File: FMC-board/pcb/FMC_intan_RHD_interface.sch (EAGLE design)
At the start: 84 parts, among them Q1 SSM3J328R, U1 4901, U2 7933, U3 ADN4663, U4 ADN4663, U5 ADN4664, U6 PDS1, U7 4901, U8 FMC_SINGLE_WIDTH_MODULE

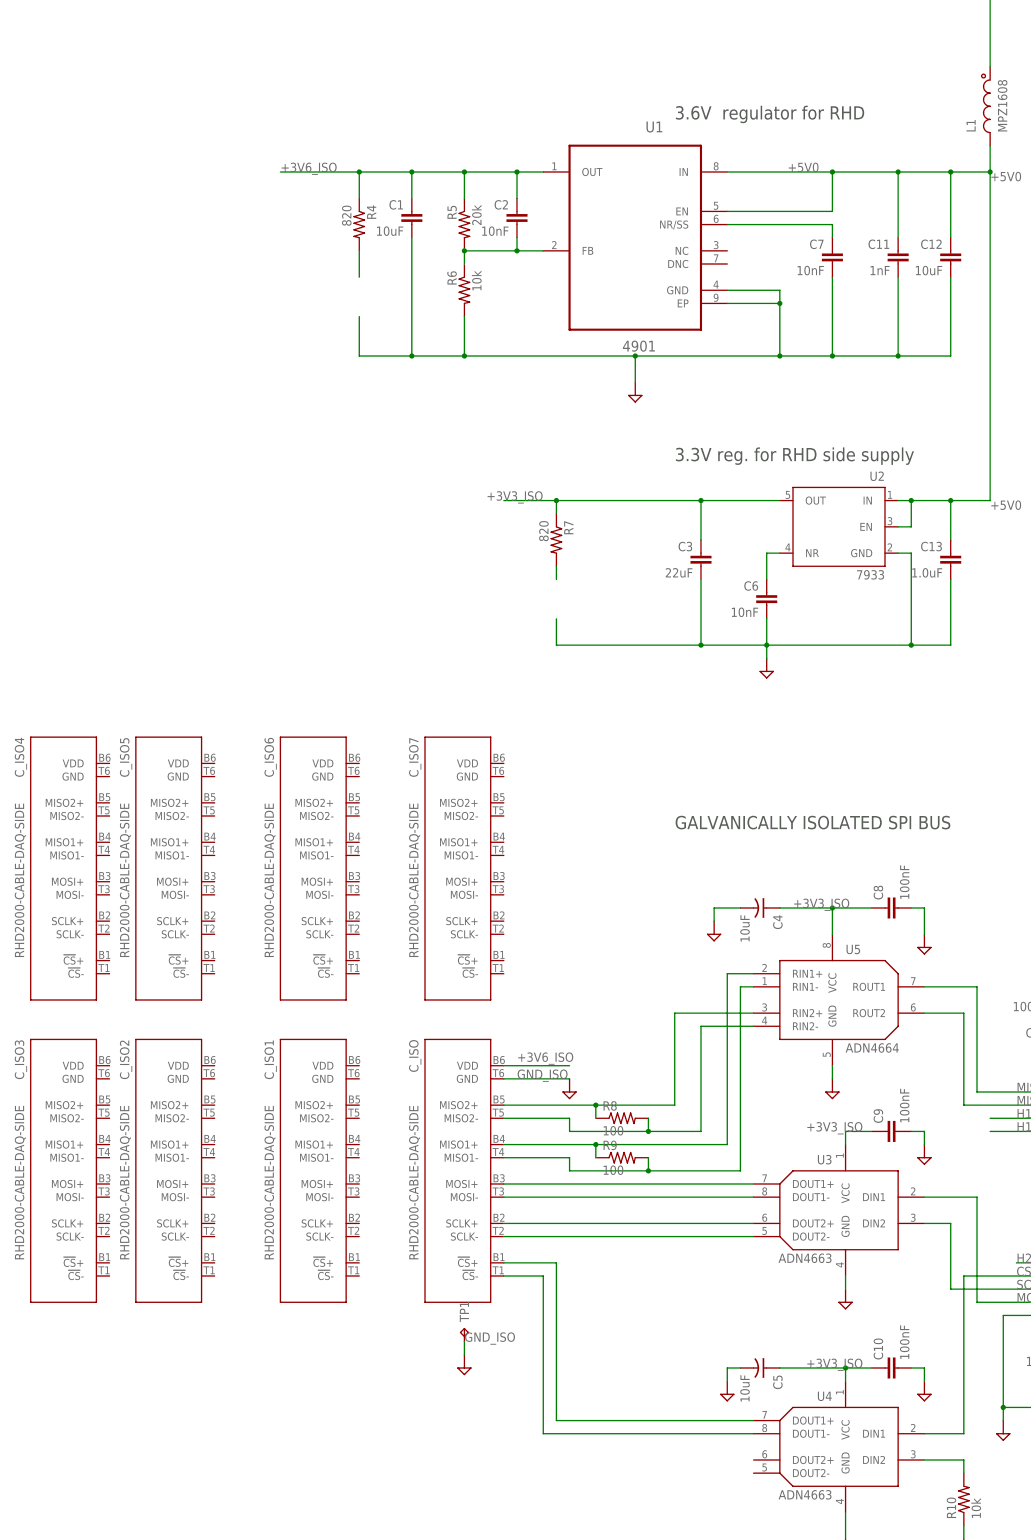
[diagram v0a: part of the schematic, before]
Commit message: added some cmos/lvds bridge components to check spacing
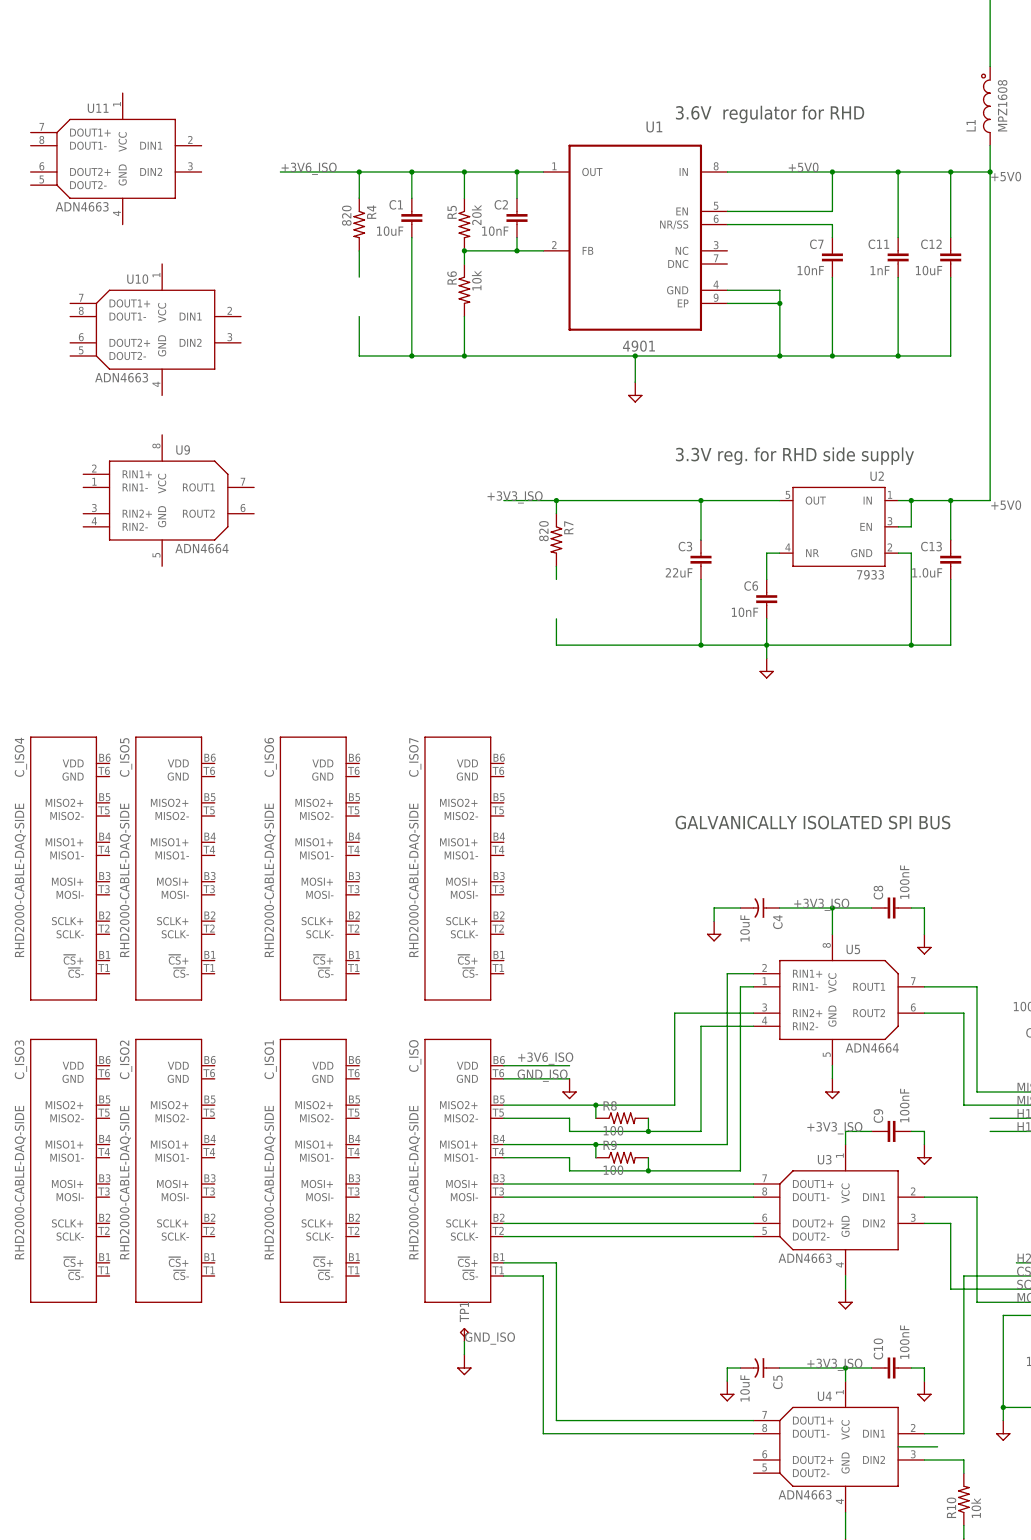
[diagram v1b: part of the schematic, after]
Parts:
- added U10, U11: ADN4663, jonnew:ADN4663_SOIC
- added U9: ADN4664, jonnew:ADN4664_SOIC
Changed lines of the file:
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@@
 <part name="DO_ISO2" library="jonnew" deviceset="ADUM3440" device="" value="ISO7640"/>
 <part name="DI_ISO2" library="jonnew" deviceset="ADUM3440" device="" value="ISO7640"/>
+<part name="U9" library="jonnew" deviceset="ADN4664" device="_SOIC" value="ADN4664"/>
+<part name="U10" library="jonnew" deviceset="ADN4663" device="_SOIC" value="ADN4663"/>
+<part name="U11" library="jonnew" deviceset="ADN4663" device="_SOIC" value="ADN4663"/>
 </parts>
 <sheets>
@@
 <instance part="DO_ISO2" gate="G$1" x="228.6" y="66.04" rot="R180"/>
 <instance part="DI_ISO2" gate="G$1" x="228.6" y="88.9"/>
+<instance part="U9" gate="G$1" x="33.02" y="287.02"/>
+<instance part="U10" gate="G$1" x="27.94" y="317.5" rot="MR0"/>
+<instance part="U11" gate="G$1" x="20.32" y="350.52" rot="MR0"/>
 </instances>
 <busses>
@@
 <pinref part="U4" gate="G$1" pin="DIN1"/>
 <wire x1="185.42" y1="109.22" x2="177.8" y2="109.22" width="0.1524" layer="91"/>
-</segment>
-</net>
+<wire x1="180.34" y1="106.68" x2="172.72" y2="106.68" width="0.1524" layer="91"/>
+</segment>
+</net>

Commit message: basic layout concept for 8 SPI interfaces on one FMC carrier
using existing parts, but utilizing both sides of the PCB
only added 4 ports for now to evaluate the basic stragety
there are a lot of traces that need to be split etc.
will have to switch to flatter DC-DC for this
also check if we can use 2 power supplies for 8 posrts or if we need to bump up the current capacity.
might be able to expand the back of the pcb outline behind the FMC a bit and stay within the vita spec?
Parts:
- removed C_ISO, C_ISO5, C_ISO6, C_ISO7: RHD2000-CABLE-DAQ-SIDE, RHD2000_eval_board:RHD2000-CABLE-DAQ-SIDE
- removed DI_ISO, DO_ISO: ISO7640, jonnew:ADUM3440
- removed TP1: GND-ISO, jonnew:TPPAD1-13
- removed TP_CS: CS, jonnew:TPTP06R
- removed TP_H1: H23, jonnew:TPTP06R
- removed TP_H2: H14, jonnew:TPTP06R
- removed TP_H3: H13, jonnew:TPTP06R
- removed TP_MISO1: MISO1, jonnew:TPTP06R
- removed TP_MISO2: MISO2, jonnew:TPTP06R
- removed TP_MOSI: MOSI, jonnew:TPTP06R
- removed TP_SCLK: SCLK, jonnew:TPTP06R
- added C33, C34, C35, C36, C37, C38, C39, C42, C43, C44, C47, C48, C49, C50: 100nF, RHD2000_eval_board:C_0603
- added C40, C41, C45, C46, C51: 10uF, jonnew:C-POL_1206
- added DI_ISO3, DI_ISO4: ISO7640, jonnew:ADUM3440
- added R1, R14, R15, R2, R3: 100, RHD2000_eval_board:R_0603
- added U12: ADN4664, jonnew:ADN4664_SOIC
- added U13, U14, U15: ADN4663, jonnew:ADN4663_SOIC
- C17: value 100nF -> 10uF; device RHD2000_eval_board:C_0603 -> jonnew:C-POL_1206
- C4, C5: value 10uF -> 100nF; device jonnew:C-POL_1206 -> RHD2000_eval_board:C_0603
- R10: value 10k -> 100; device jonnew:R_0603 -> RHD2000_eval_board:R_0603
- U11, U3: value ADN4663 -> ADN4664; device jonnew:ADN4663_SOIC -> jonnew:ADN4664_SOIC
- U9: value ADN4664 -> ADN4663; device jonnew:ADN4664_SOIC -> jonnew:ADN4663_SOIC
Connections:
- removed net CS+_ISOLATED: C_ISO.!CS!+, U4.DOUT1+
- removed net CS-_ISOLATED: C_ISO.!CS!-, U4.DOUT1-
- removed net MISO1+_ISOLATED: C_ISO.MISO1+, R9.1, U5.RIN1+
- removed net MISO1-_ISOLATED: C_ISO.MISO1-, R9.2, U5.RIN1-
- removed net MISO2+_ISOLATED: C_ISO.MISO2+, R8.1, U5.RIN2+
- removed net MISO2-_ISOLATED: C_ISO.MISO2-, R8.2, U5.RIN2-
- removed net N$5: R10.2, U4.DIN2
- new net CS+_ISOLATED1: C_ISO1.!CS!+, U14.DOUT1+
- new net CS+_ISOLATED2: C_ISO2.!CS!+
- new net CS+_ISOLATED3: C_ISO3.!CS!+, U10.DOUT1+
- new net CS+_ISOLATED4: C_ISO4.!CS!+
- new net CS-_ISOLATED1: C_ISO1.!CS!-, U14.DOUT1-
- new net CS-_ISOLATED2: C_ISO2.!CS!-
- new net CS-_ISOLATED3: C_ISO3.!CS!-, U10.DOUT1-
- new net CS-_ISOLATED4: C_ISO4.!CS!-
- new net MISO1+_ISOLATED1: C_ISO1.MISO1+, R2.1, U12.RIN1+
- new net MISO1+_ISOLATED2: C_ISO2.MISO1+, R9.1, U3.RIN1+
- new net MISO1+_ISOLATED3: C_ISO3.MISO1+, R10.1, U5.RIN1+
- new net MISO1+_ISOLATED4: C_ISO4.MISO1+, R15.1, U11.RIN1+
- new net MISO1-_ISOLATED1: C_ISO1.MISO1-, R2.2, U12.RIN1-
- new net MISO1-_ISOLATED2: C_ISO2.MISO1-, R9.2, U3.RIN1-
- new net MISO1-_ISOLATED3: C_ISO3.MISO1-, R10.2, U5.RIN1-
- new net MISO1-_ISOLATED4: C_ISO4.MISO1-, R15.2, U11.RIN1-
- new net MISO2+_ISOLATED1: C_ISO1.MISO2+, R1.1, U12.RIN2+
- new net MISO2+_ISOLATED2: C_ISO2.MISO2+, R8.1, U3.RIN2+
- new net MISO2+_ISOLATED3: C_ISO3.MISO2+, R3.1, U5.RIN2+
- new net MISO2+_ISOLATED4: C_ISO4.MISO2+, R14.1, U11.RIN2+
- new net MISO2-_ISOLATED1: C_ISO1.MISO2-, R1.2, U12.RIN2-
- new net MISO2-_ISOLATED2: C_ISO2.MISO2-, R8.2, U3.RIN2-
- new net MISO2-_ISOLATED3: C_ISO3.MISO2-, R3.2, U5.RIN2-
- new net MISO2-_ISOLATED4: C_ISO4.MISO2-, R14.2, U11.RIN2-
- new net N$11: C_ISO1.MOSI-, U13.DOUT1-
- new net N$14: C_ISO1.SCLK+, U13.DOUT2+
- new net N$17: C_ISO1.SCLK-, U13.DOUT2-
- new net N$18: C_ISO3.MOSI-, U9.DOUT1-
- new net N$19: C_ISO3.SCLK+, U9.DOUT2+
- new net N$2: C_ISO3.MOSI+, U9.DOUT1+
- new net N$20: C_ISO3.SCLK-, U9.DOUT2-
- new net N$21: C_ISO4.MOSI+, U15.DOUT1+
- new net N$22: C_ISO4.MOSI-, U15.DOUT1-
- new net N$23: C_ISO4.SCLK+, U15.DOUT2+
- new net N$24: C_ISO4.SCLK-, U15.DOUT2-
- new net N$9: C_ISO1.MOSI+, U13.DOUT1+
- net +3V3: now also C33.2, C37.2, C4.2, C42.2, C47.2, C8.2, DI_ISO1.VDD2, DI_ISO1.VE2, DI_ISO2.VDD2, DI_ISO2.VE2, DI_ISO3.VDD2, DI_ISO3.VE2, DI_ISO4.VDD2, DI_ISO4.VE2, DO_ISO1.VDD1, DO_ISO2.VDD1; no longer C17.2, C18.2, DI_ISO.VDD2, DI_ISO.VE2, DO_ISO.VDD1
- net +3V3_ISO: now also C15.1, C17.+, C18.1, C34.1, C35.1, C36.1, C38.2, C39.2, C40.+, C41.+, C43.2, C44.2, C45.+, C46.+, C48.1, C49.1, C5.1, C50.2, C51.+, DI_ISO1.VDD1, DI_ISO2.VDD1, DI_ISO3.VDD1, DI_ISO4.VDD1, DO_ISO1.VDD2, DO_ISO1.VE2, DO_ISO2.VDD2, DO_ISO2.VE2, U10.VCC, U11.VCC, U12.VCC, U13.VCC, U14.VCC, U15.VCC, U9.VCC; no longer C15.2, C4.+, C5.+, C8.1, DI_ISO.VDD1, DO_ISO.VDD2, DO_ISO.VE2
- net +3V6_ISO: now also C_ISO1.VDD, C_ISO2.VDD, C_ISO3.VDD, C_ISO4.VDD; no longer C_ISO.VDD
- net CS: now also DO_ISO1.VIC, DO_ISO2.VIC; no longer DO_ISO.VIC, TP_CS.TP
- net CS_ISO: now also DO_ISO1.VOC, DO_ISO2.VOC, U10.DIN1, U14.DIN1; no longer DO_ISO.VOC, U4.DIN1
- net GND: now also C33.1, C37.1, C4.1, C42.1, C47.1, C8.1, DI_ISO1.GND2, DI_ISO2.GND2, DI_ISO3.GND2, DI_ISO4.GND2, DO_ISO1.GND1, DO_ISO2.GND1; no longer C17.1, C18.1, DI_ISO.GND2, DO_ISO.GND1
- net GND_ISO: now also C15.2, C17.-, C18.2, C34.2, C35.2, C36.2, C38.1, C39.1, C40.-, C41.-, C43.1, C44.1, C45.-, C46.-, C48.2, C49.2, C5.2, C50.1, C51.-, C_ISO1.GND, C_ISO2.GND, C_ISO3.GND, C_ISO4.GND, DI_ISO1.GND1, DI_ISO2.GND1, DI_ISO3.GND1, DI_ISO4.GND1, DO_ISO1.GND2, DO_ISO2.GND2, U10.GND, U11.GND, U12.GND, U13.GND, U14.GND, U15.GND, U9.GND; no longer C15.1, C4.-, C5.-, C8.2, C_ISO.GND, DI_ISO.GND1, DO_ISO.GND2, R10.1, TP1.TP
- net H13: now also DI_ISO1.VOD, DI_ISO2.VOD, DI_ISO3.VOD, DI_ISO4.VOD; no longer DI_ISO.VOD, TP_H3.TP
- net H13_ISO: now also DI_ISO1.VID, DI_ISO2.VID, DI_ISO3.VID, DI_ISO4.VID; no longer DI_ISO.VID
- net H14: now also DI_ISO1.VOC, DI_ISO2.VOC, DI_ISO3.VOC, DI_ISO4.VOC; no longer DI_ISO.VOC, TP_H2.TP
- net H14_ISO: now also DI_ISO1.VIC, DI_ISO2.VIC, DI_ISO3.VIC, DI_ISO4.VIC; no longer DI_ISO.VIC
- net H23: now also DO_ISO1.VID, DO_ISO2.VID; no longer DO_ISO.VID, TP_H1.TP
- net H23_ISO: now also DO_ISO1.VOD, DO_ISO2.VOD, U10.DIN2, U14.DIN2; no longer DO_ISO.VOD
- net MISO1: now also DI_ISO1.VOA, DI_ISO2.VOA, DI_ISO3.VOA, DI_ISO4.VOA; no longer DI_ISO.VOA, TP_MISO1.TP
- net MISO1_ISO: now also DI_ISO1.VIA, DI_ISO2.VIA, DI_ISO3.VIA, DI_ISO4.VIA, U11.ROUT1, U12.ROUT1, U3.ROUT1; no longer DI_ISO.VIA
- net MISO2: now also DI_ISO1.VOB, DI_ISO2.VOB, DI_ISO3.VOB, DI_ISO4.VOB; no longer DI_ISO.VOB, TP_MISO2.TP
- net MISO2_ISO: now also DI_ISO1.VIB, DI_ISO2.VIB, DI_ISO3.VIB, DI_ISO4.VIB, U11.ROUT2, U12.ROUT2, U3.ROUT2; no longer DI_ISO.VIB
- net MOSI: now also DO_ISO1.VIA, DO_ISO2.VIA; no longer DO_ISO.VIA, TP_MOSI.TP
- net MOSI_ISO: now also DO_ISO1.VOA, DO_ISO2.VOA, U13.DIN1, U15.DIN1, U4.DIN1, U9.DIN1; no longer DO_ISO.VOA, U3.DIN1
- net N$12: now also C_ISO2.MOSI+, U4.DOUT1+; no longer C_ISO.MOSI+, U3.DOUT1+
- net N$13: now also C_ISO2.MOSI-, U4.DOUT1-; no longer C_ISO.MOSI-, U3.DOUT1-
- net N$15: now also C_ISO2.SCLK+, U4.DOUT2+; no longer C_ISO.SCLK+, U3.DOUT2+
- net N$16: now also C_ISO2.SCLK-, U4.DOUT2-; no longer C_ISO.SCLK-, U3.DOUT2-
- net SCLK: now also DO_ISO1.VIB, DO_ISO2.VIB; no longer DO_ISO.VIB, TP_SCLK.TP
- net SCLK_ISO: now also DO_ISO1.VOB, DO_ISO2.VOB, U13.DIN2, U15.DIN2, U4.DIN2, U9.DIN2; no longer DO_ISO.VOB, U3.DIN2
